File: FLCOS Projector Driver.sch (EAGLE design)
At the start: 63 parts, among them IC2 LM3414, IC3 MIC5219BM5, IC4 MIC5219BM5, IC5 LM3414, IC6 LM3414, Q1 14.31818MHz, Q3 12MHz, T2 S8050, T3 S8050, U1 TVP5150-NTSC_DECODER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

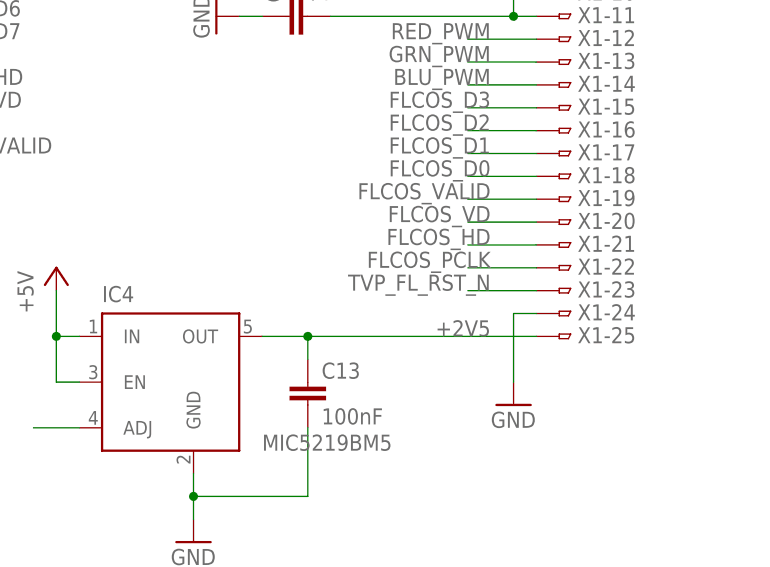
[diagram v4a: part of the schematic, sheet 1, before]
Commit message: GPIO0 to reset the TVP, ESP_EN_N to reset the FLCOS
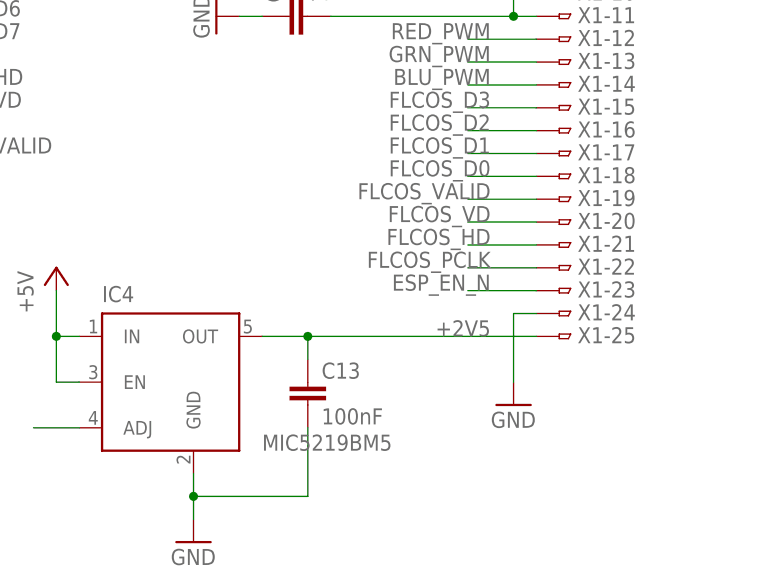
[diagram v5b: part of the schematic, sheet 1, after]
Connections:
- net ESP_EN_N: now also X1-23.1
- net TVP_FL_RST_N: no longer X1-23.1
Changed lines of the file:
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@@
 <label x="30.48" y="60.96" size="1.778" layer="95" rot="MR0"/>
-</segment>
-<segment>
-<pinref part="X1" gate="-23" pin="1"/>
-<wire x1="139.7" y1="17.78" x2="132.08" y2="17.78" width="0.1524" layer="91"/>
-<label x="134.62" y="17.78" size="1.778" layer="95" rot="MR0"/>
 </segment>
 </net>
@@
 </segment>
 </net>
+<net name="ESP_EN_N" class="0">
+<segment>
+<pinref part="X1" gate="-23" pin="1"/>
+<wire x1="139.7" y1="17.78" x2="132.08" y2="17.78" width="0.1524" layer="91"/>
+<label x="134.62" y="17.78" size="1.778" layer="95" rot="MR0"/>
+</segment>
+</net>

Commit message: README update
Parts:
- added R12: 2K2, rcl:R-EU_R0603
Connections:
- net FLCOS_D7: now also R12.2
- net GND: now also R12.1
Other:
- note added: "<- Set I2C Addr to 0xB8"
- moved on the sheet: C13, C22, IC4, R11, X1-1, X1-10, X1-11, X1-12, X1-13, X1-14, X1-15, X1-16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

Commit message: Updated README
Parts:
- renumbered JP2 to CVBS
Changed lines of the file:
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@@
 <part name="GND25" library="supply1" deviceset="GND" device=""/>
 <part name="Q1" library="crystal" deviceset="CRYSTAL" device="CTS406" value="14.31818MHz"/>
-<part name="JP2" library="pinhead" deviceset="PINHD-1X3" device="" package3d_urn="urn:adsk.eagle:package:22458/2"/>
+<part name="CVBS" library="pinhead" deviceset="PINHD-1X3" device="" package3d_urn="urn:adsk.eagle:package:22458/2"/>
 <part name="GND26" library="supply1" deviceset="GND" device=""/>
 <part name="C22" library="rcl" deviceset="C-EU" device="C0603" value="100nF"/>
@@
 <instance part="GND25" gate="1" x="-20.32" y="30.48" rot="R90"/>
 <instance part="Q1" gate="G$1" x="7.62" y="53.34" rot="R90"/>
-<instance part="JP2" gate="A" x="-71.12" y="22.86" rot="MR0"/>
+<instance part="CVBS" gate="A" x="-71.12" y="22.86" rot="MR0"/>
 <instance part="GND26" gate="1" x="-63.5" y="15.24"/>
 <instance part="C22" gate="G$1" x="132.08" y="53.34" rot="R90"/>
@@
 </segment>
 <segment>
-<pinref part="JP2" gate="A" pin="3"/>
+<pinref part="CVBS" gate="A" pin="3"/>
 <pinref part="GND26" gate="1" pin="GND"/>
 <wire x1="-68.58" y1="20.32" x2="-63.5" y2="20.32" width="0.1524" layer="91"/>
@@
 <pinref part="R7" gate="G$1" pin="1"/>
 <wire x1="-50.8" y1="38.1" x2="-58.42" y2="38.1" width="0.1524" layer="91"/>
-<pinref part="JP2" gate="A" pin="1"/>
+<pinref part="CVBS" gate="A" pin="1"/>
 <wire x1="-58.42" y1="38.1" x2="-58.42" y2="25.4" width="0.1524" layer="91"/>
 <wire x1="-58.42" y1="25.4" x2="-68.58" y2="25.4" width="0.1524" layer="91"/>
@@
 <pinref part="R9" gate="G$1" pin="1"/>
 <wire x1="-50.8" y1="10.16" x2="-58.42" y2="10.16" width="0.1524" layer="91"/>
-<pinref part="JP2" gate="A" pin="2"/>
+<pinref part="CVBS" gate="A" pin="2"/>
 <wire x1="-58.42" y1="10.16" x2="-58.42" y2="22.86" width="0.1524" layer="91"/>
 <wire x1="-58.42" y1="22.86" x2="-68.58" y2="22.86" width="0.1524" layer="91"/>
